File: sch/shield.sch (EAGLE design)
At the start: 19 parts, among them IC1 LM1881

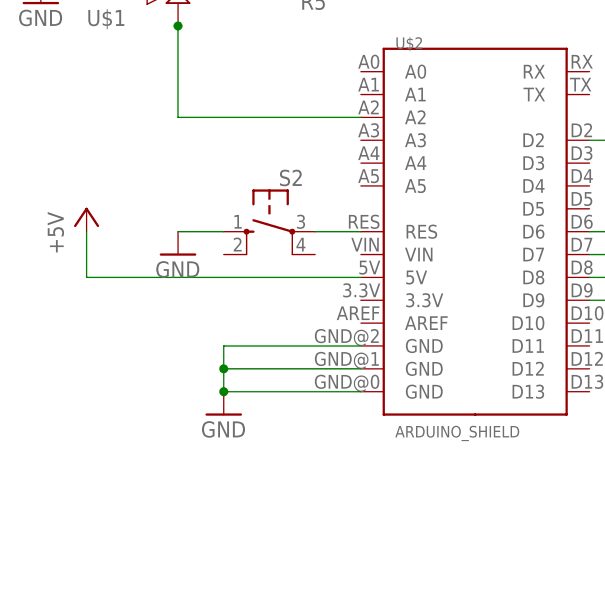
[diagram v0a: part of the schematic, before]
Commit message: sch: Remove unneeded connections
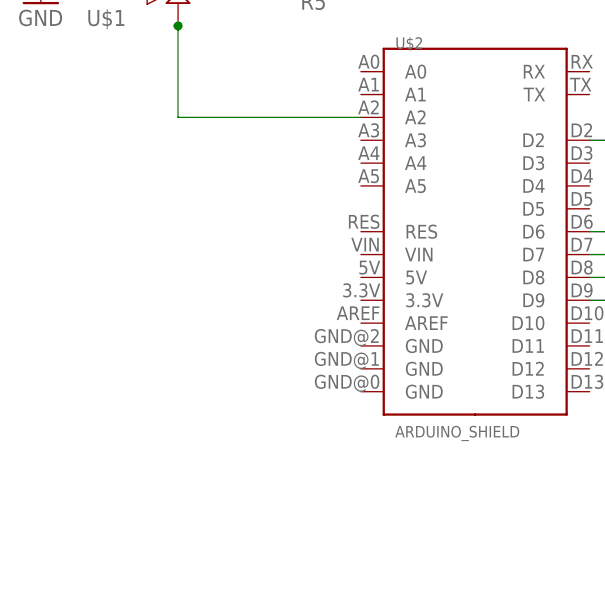
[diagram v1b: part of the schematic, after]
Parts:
- removed S2: SWITCH-TACTSWITCH-TACT-B, nootropicdesign:SWITCH-TACTSWITCH-TACT-B
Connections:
- removed net RESET: S2.P, U$2.RES
- net +5V: no longer U$2.5V
- net GND: no longer S2.S, U$2.GND@0, U$2.GND@1, U$2.GND@2
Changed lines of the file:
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@@
 <part name="GND2" library="supply1" deviceset="GND" device=""/>
 <part name="GND3" library="supply1" deviceset="GND" device=""/>
-<part name="GND4" library="supply1" deviceset="GND" device=""/>
 <part name="D1" library="nootropicdesign" deviceset="1N4148" device=""/>
 <part name="C2" library="nootropicdesign" deviceset="CAP" device="SMALL" value=".1uF"/>
@@
 <part name="GND8" library="supply1" deviceset="GND" device=""/>
 <part name="P+1" library="supply1" deviceset="+5V" device=""/>
-<part name="GND9" library="supply1" deviceset="GND" device=""/>
 <part name="U$1" library="nootropicdesign" deviceset="POT" device=""/>
 <part name="S3" library="nootropicdesign" deviceset="SWITCH-DPDT" device=""/>
@@
 <part name="R5" library="nootropicdesign" deviceset="R-US" device="" value="20K"/>
 <part name="P+2" library="supply1" deviceset="+5V" device=""/>
-<part name="S2" library="nootropicdesign" deviceset="SWITCH-TACT" device="SWITCH-TACT-B"/>
 <part name="U$5" library="nootropicdesign" deviceset="TRIMPOT" device="TIGHT"/>
-<part name="P+3" library="supply1" deviceset="+5V" device=""/>
 </parts>
 <sheets>
@@
 <instance part="GND2" gate="1" x="30.48" y="-12.7"/>
 <instance part="GND3" gate="1" x="15.24" y="60.96"/>
-<instance part="GND4" gate="1" x="-96.52" y="10.16"/>
 <instance part="D1" gate="G$1" x="0" y="27.94"/>
 <instance part="C2" gate="G$1" x="38.1" y="30.48" rot="R90"/>
@@
 <instance part="GND8" gate="1" x="-116.84" y="55.88"/>
 <instance part="P+1" gate="1" x="71.12" y="45.72"/>
-<instance part="GND9" gate="1" x="-101.6" y="27.94"/>
 <instance part="U$1" gate="G$1" x="-106.68" y="58.42" rot="R270"/>
 <instance part="S3" gate="G$1" x="2.54" y="50.8" rot="MR0"/>
@@
 <instance part="R5" gate="G$1" x="-88.9" y="58.42" rot="R180"/>
 <instance part="P+2" gate="1" x="-81.28" y="66.04"/>
-<instance part="S2" gate="G$1" x="-91.44" y="30.48" rot="MR0"/>
 <instance part="U$5" gate="G$1" x="99.06" y="7.62" rot="R90"/>
-<instance part="P+3" gate="1" x="-111.76" y="33.02"/>
 </instances>
 <busses>
@@
 <pinref part="GND2" gate="1" pin="GND"/>
 <pinref part="INPUT" gate="G$1" pin="GND"/>
-</segment>
-<segment>
-<wire x1="-96.52" y1="17.78" x2="-96.52" y2="15.24" width="0.1524" layer="91"/>
-<wire x1="-96.52" y1="15.24" x2="-96.52" y2="12.7" width="0.1524" layer="91"/>
-<wire x1="-81.28" y1="17.78" x2="-96.52" y2="17.78" width="0.1524" layer="91"/>
-<wire x1="-81.28" y1="12.7" x2="-96.52" y2="12.7" width="0.1524" layer="91"/>
-<wire x1="-81.28" y1="15.24" x2="-96.52" y2="15.24" width="0.1524" layer="91"/>
-<junction x="-96.52" y="12.7"/>
-<junction x="-96.52" y="15.24"/>
-<pinref part="GND4" gate="1" pin="GND"/>
-<pinref part="U$2" gate="G$1" pin="GND@2"/>
-<pinref part="U$2" gate="G$1" pin="GND@1"/>
-<pinref part="U$2" gate="G$1" pin="GND@0"/>
 </segment>
 <segment>
@@
 </segment>
 <segment>
-<wire x1="-96.52" y1="30.48" x2="-101.6" y2="30.48" width="0.1524" layer="91"/>
-<pinref part="GND9" gate="1" pin="GND"/>
-<pinref part="S2" gate="G$1" pin="S"/>
-</segment>
-<segment>
 <pinref part="R6" gate="G$1" pin="2"/>
 <pinref part="GND10" gate="1" pin="GND"/>
@@
 <pinref part="U$1" gate="G$1" pin="WIPER@1"/>
 <pinref part="U$1" gate="G$1" pin="WIPER@2"/>
-</segment>
-</net>
-<net name="RESET" class="0">
-<segment>
-<wire x1="-86.36" y1="30.48" x2="-81.28" y2="30.48" width="0.1524" layer="91"/>
-<pinref part="U$2" gate="G$1" pin="RES"/>
-<pinref part="S2" gate="G$1" pin="P"/>
 </segment>
 </net>
@@
 <wire x1="-81.28" y1="58.42" x2="-83.82" y2="58.42" width="0.1524" layer="91"/>
 </segment>
-<segment>
-<pinref part="U$2" gate="G$1" pin="5V"/>
-<wire x1="-81.28" y1="25.4" x2="-111.76" y2="25.4" width="0.1524" layer="91"/>
-<wire x1="-111.76" y1="25.4" x2="-111.76" y2="30.48" width="0.1524" layer="91"/>
-<pinref part="P+3" gate="1" pin="+5V"/>
-</segment>
-</net>
+</net>
